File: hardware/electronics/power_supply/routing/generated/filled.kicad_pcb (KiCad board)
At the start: 6 copper layers, 84 x 38 mm, 161 parts, among them J1 Header2, J2 Header6, J3 Header2, J4 Header6, J5 Header2, U1 LT3471EDD#PBF, U10 LT3090IDD#PBF, U11 LT3090IDD#PBF, U12 LT1634AIS8-2.5#PBF, U13 LT3471EDD#PBF, U2 TPS62933FDRLR, U3 TPS62933FDRLR, U4 REF5025EIDR, U5 OPA4192ID, U6 OPA2192ID, U7 LT3080IMS8E#PBF, U8 LT3080IQ#PBF, U9 LT3080IMS8E#PBF

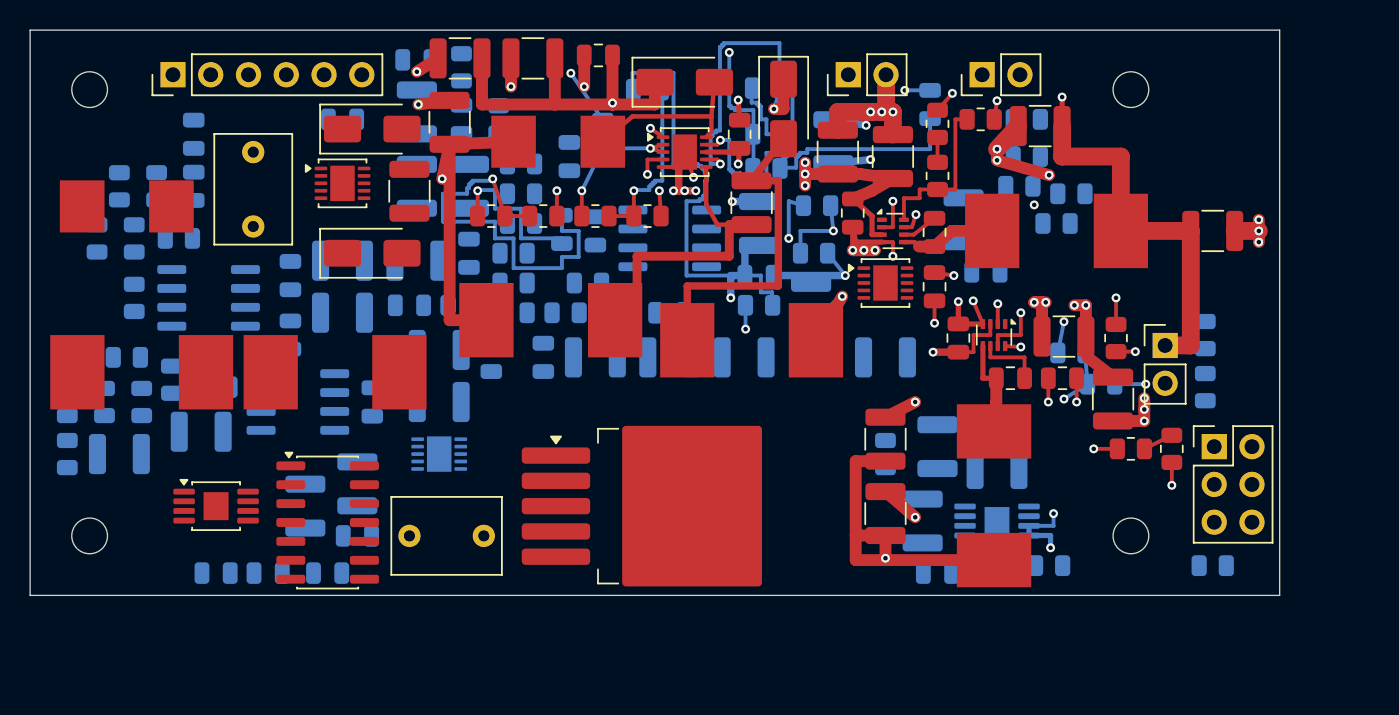
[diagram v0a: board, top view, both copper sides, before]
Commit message: Preserve standalone power routing, E25 placement and A11 housing
Close main-supply routing and add source-verified disconnect placement, housing clearances, harness screens and regression tests. Preserve the verified review packages and retain explicit unfinished routing, 5 V distribution and physical qualification records.
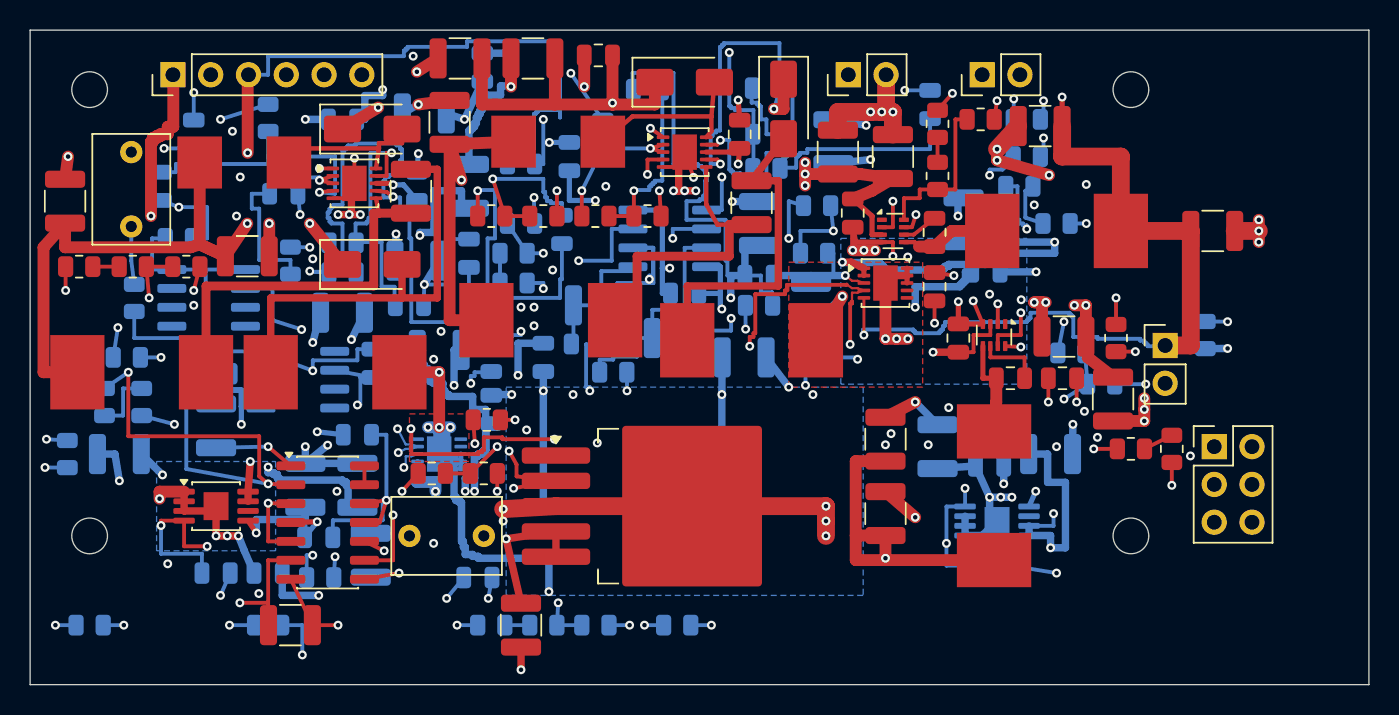
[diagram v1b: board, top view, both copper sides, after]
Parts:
- C2, C3, C39, C41, R1, R17, R2, R3, R30, R31: moved to F.Cu
- moved R32 60.9 mm to (119.5, 136.8), turned to 0 degrees
- moved R31 49.4 mm to (130.5, 129.8)
- moved C44 42.5 mm to (122.9, 135.3), turned to 90 degrees
- moved R30 42.0 mm to (127.0, 129.8)
- moved R42 33.1 mm to (139.2, 123.0)
- moved R28 31.5 mm to (116.0, 140.0)
- moved C39 31.2 mm to (117.5, 140.0), turned to 180 degrees
- moved R1 29.0 mm to (103.3, 115.9), turned to 0 degrees
- moved R2 26.5 mm to (106.9, 115.9), turned to 0 degrees
- moved R29 23.7 mm to (143.5, 140.0)
- moved R25 22.7 mm to (131.0, 140.0)
- moved R27 22.6 mm to (138.0, 140.0), turned to 0 degrees
- moved C40 22.0 mm to (130.1, 136.8)
- moved R17 21.4 mm to (130.7, 126.2), turned to 0 degrees
- moved R26 21.1 mm to (134.5, 140.0)
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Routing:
- net /AGND: track 357.3 -> 1213.3 mm, vias 43 -> 96
- net /RAW_N22: track 0.00 -> 251.5 mm, vias 0 -> 14
- net /RAW_P22: track 0.00 -> 194.9 mm, vias 0 -> 12
- net /P12_SRC: track 0.00 -> 178.7 mm, vias 0 -> 12
- net /5V_DIG_SRC: track 98.1 -> 274.6 mm, vias 3 -> 9
- net /N19_SRC: track 0.00 -> 130.8 mm, vias 0 -> 6
- net /V5_REG_SET: track 0.00 -> 110.7 mm, vias 0 -> 4
- net /RAW_P17: track 56.5 -> 166.9 mm, vias 2 -> 10
- net /N12_SRC: track 0.00 -> 104.3 mm, vias 0 -> 4
- net /VIN_PROTECTED: track 162.6 -> 256.8 mm, vias 8 -> 11
- net /N12_SET: track 0.00 -> 78.3 mm, vias 0 -> 6
- net /NREF_FILTER: track 0.00 -> 78.1 mm, vias 0 -> 4
- net /P19_SRC: track 0.00 -> 69.8 mm, vias 0 -> 8
- net /N12_FB: track 0.00 -> 68.8 mm, vias 0 -> 7
- net /P12_SET: track 0.00 -> 61.0 mm, vias 0 -> 5
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- added copper zone on B.Cu, net /P12_SRC
- added copper zone on B.Cu, net /P19_SRC
- added copper zone on B.Cu, net /RAW_N17
- added copper zone on F.Cu, net /RAW_N17
- added copper zone on F.Cu, net /RAW_N22
- added copper zone on In4.Cu, net /V5_REG_SRC
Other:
- board size 84 x 38 mm -> 90 x 44 mm
